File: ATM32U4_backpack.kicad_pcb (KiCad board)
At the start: 2 copper layers, 27 x 50.5 mm, 41 parts, among them J1 SPI 3V3, J2 WS2812, J3 UART, J4 USB_B_Micro, J5 I2C 5V, J6 ENC, J7 CS3V3, U1 LM3480-3.3, U2 TXB0104PW, U4 ATmega32U4-AU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

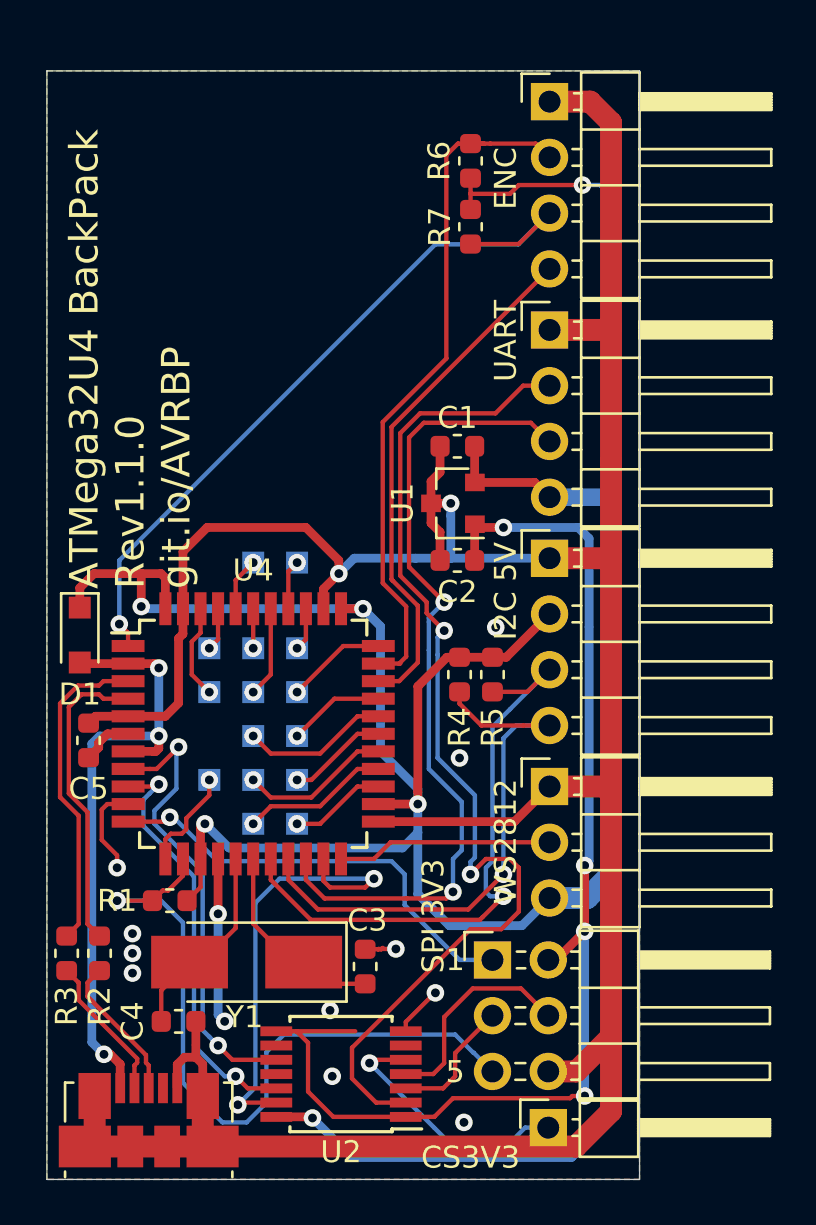
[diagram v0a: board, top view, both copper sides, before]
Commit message: made the wiggly lines more pretty
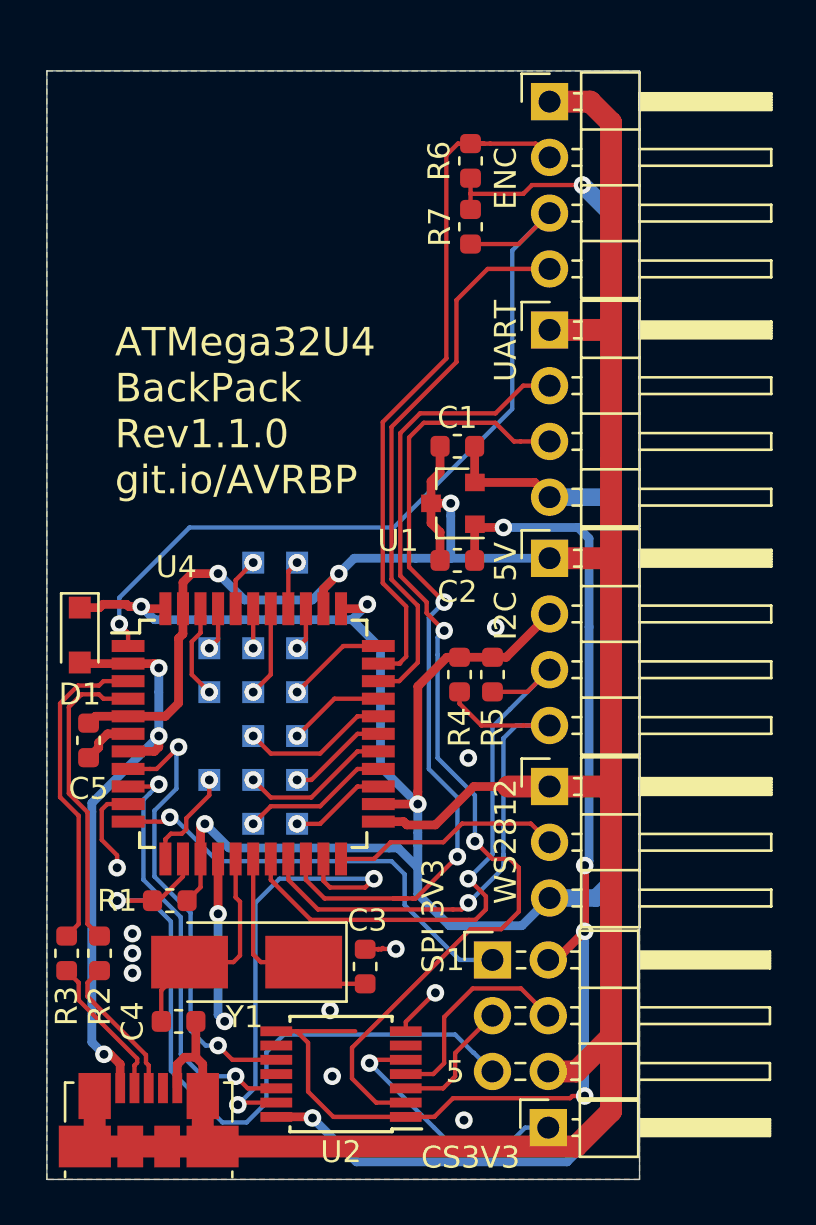
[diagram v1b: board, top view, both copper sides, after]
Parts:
- moved G*** 1.10 mm to (39.7, 76.1) (x2)
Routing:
- net +5V: track 149.8 -> 146.2 mm
- net /ENC_A: track 34.4 -> 37.6 mm
- net GND: track 163.1 -> 161.3 mm, vias 14 -> 15
- net /TX-3V3: track 48.7 -> 46.9 mm
- net /ENC_SW: track 23.6 -> 25.2 mm
- net VBUS: track 28.4 -> 26.8 mm
- net Net-(C4-Pad2): track 9.13 -> 10.1 mm
- net Net-(C3-Pad1): track 9.18 -> 10.0 mm
- net /WS2812: track 9.81 -> 10.5 mm
- net /SCK-5V: track 19.1 -> 19.7 mm
